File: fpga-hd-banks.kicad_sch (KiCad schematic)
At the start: 16 parts, among them Q4 BSS138PW, Q5 BSS138PW, Q6 BSS138PW, Q7 BSS138PW, Q8 BSS138PW, U34 XCAU25P-2FFVB676I

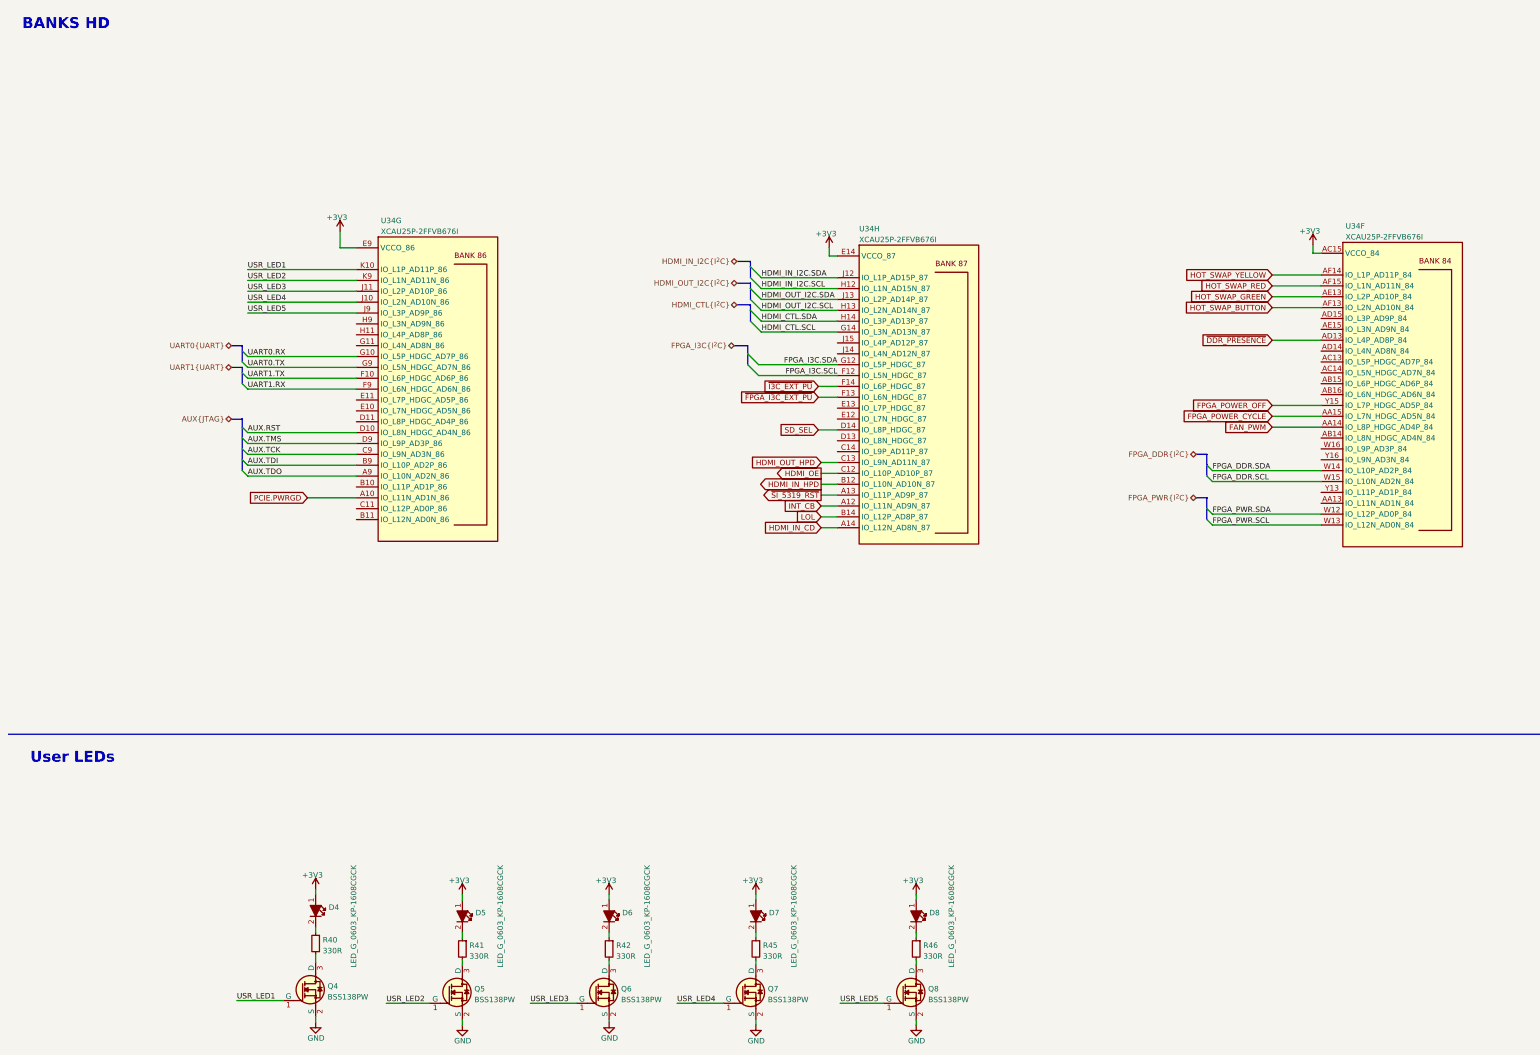
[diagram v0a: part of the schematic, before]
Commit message: [#67725] Clean-up fpga-hd-banks sheet
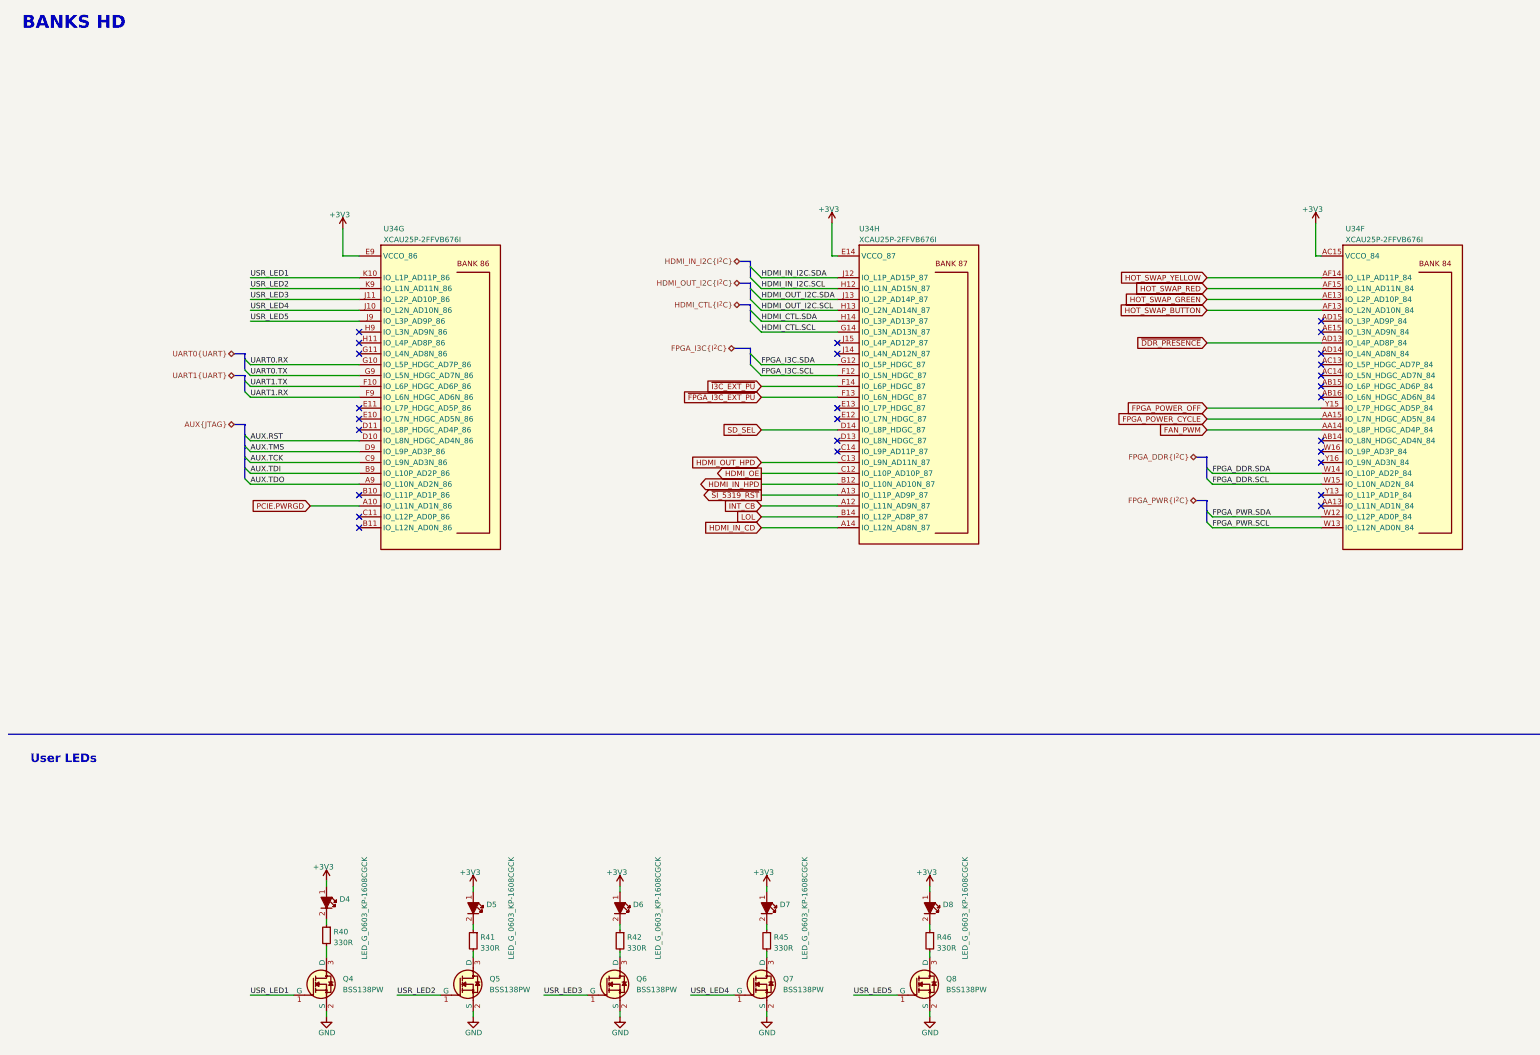
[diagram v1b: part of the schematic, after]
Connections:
- no-connect marks 0 -> 27
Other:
- moved on the sheet: D4, D5, D6, D7, D8, R40, R41, R42, R45, R46, U34F, U34G

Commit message: [#68016] Clean-up the schematic
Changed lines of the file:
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@@
   (title_block
     (title "RDIMM DDR5 Tester")
-    (date "2024-09-26")
+    (date "2024-10")
     (rev "2.0.0")
     (comment 1 "www.antmicro.com")
@@
     (stroke (width 0) (type default))
   )
-  (polyline (pts (xy 12.065 184.15) (xy 407.67 184.15))
-    (stroke (width 0) (type default))
-  )
+  (polyline (pts (xy 12.7 184.15) (xy 407.67 184.15))
+    (stroke (width 0) (type default))
+  )

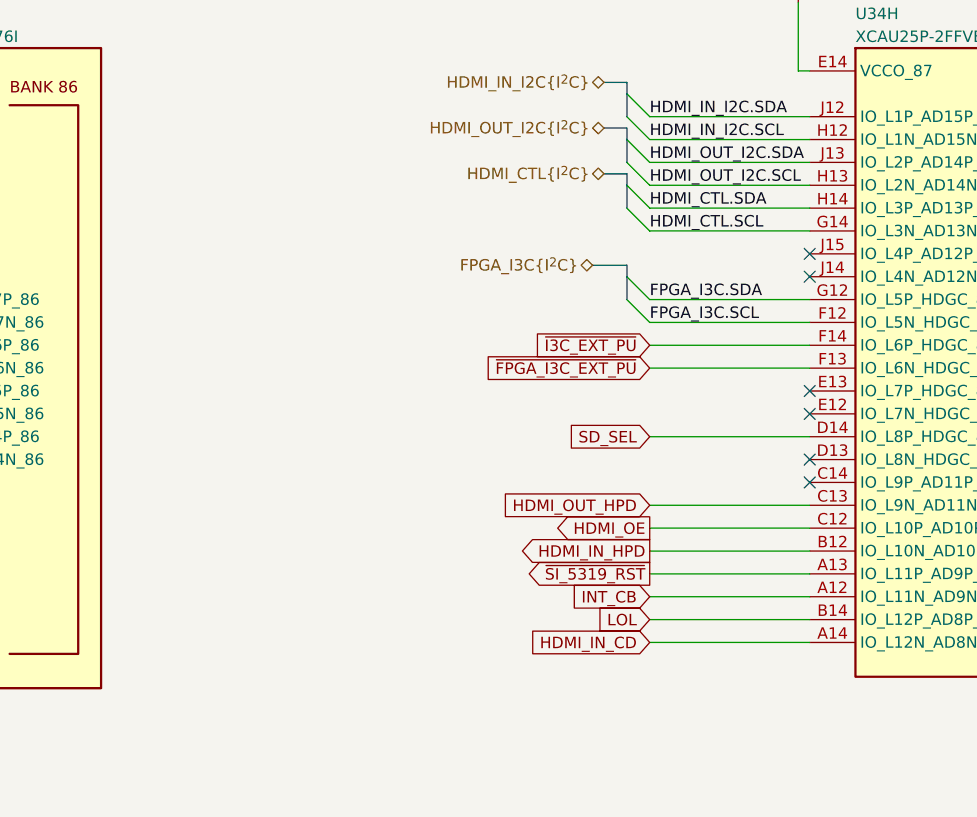
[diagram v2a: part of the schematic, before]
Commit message: [#67408] Update layout for I3C, SDcard and HDMI aux signals
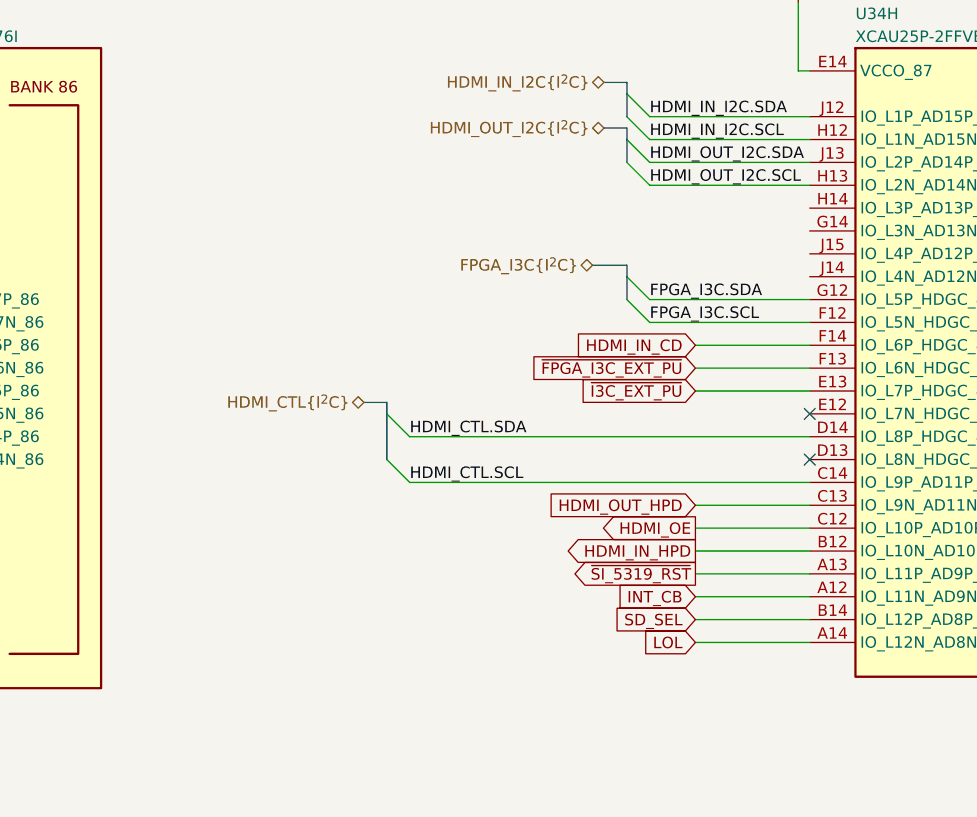
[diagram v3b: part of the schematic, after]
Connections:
- net HDMI_CTL.SCL: now also U34.C14 (IO_L9P_AD11P_87); no longer U34.G14 (IO_L3N_AD13N_87)
- net HDMI_CTL.SDA: now also U34.D14 (IO_L8P_HDGC_87); no longer U34.H14 (IO_L3P_AD13P_87)
- net HDMI_IN_CD: now also U34.F14 (IO_L6P_HDGC_87); no longer U34.A14 (IO_L12N_AD8N_87)
- net LOL: now also U34.A14 (IO_L12N_AD8N_87); no longer U34.B14 (IO_L12P_AD8P_87)
- net SD_SEL: now also U34.B14 (IO_L12P_AD8P_87); no longer U34.D14 (IO_L8P_HDGC_87)
- net ~{I3C_EXT_PU}: now also U34.E13 (IO_L7P_HDGC_87); no longer U34.F14 (IO_L6P_HDGC_87)
- no-connect marks 27 -> 23

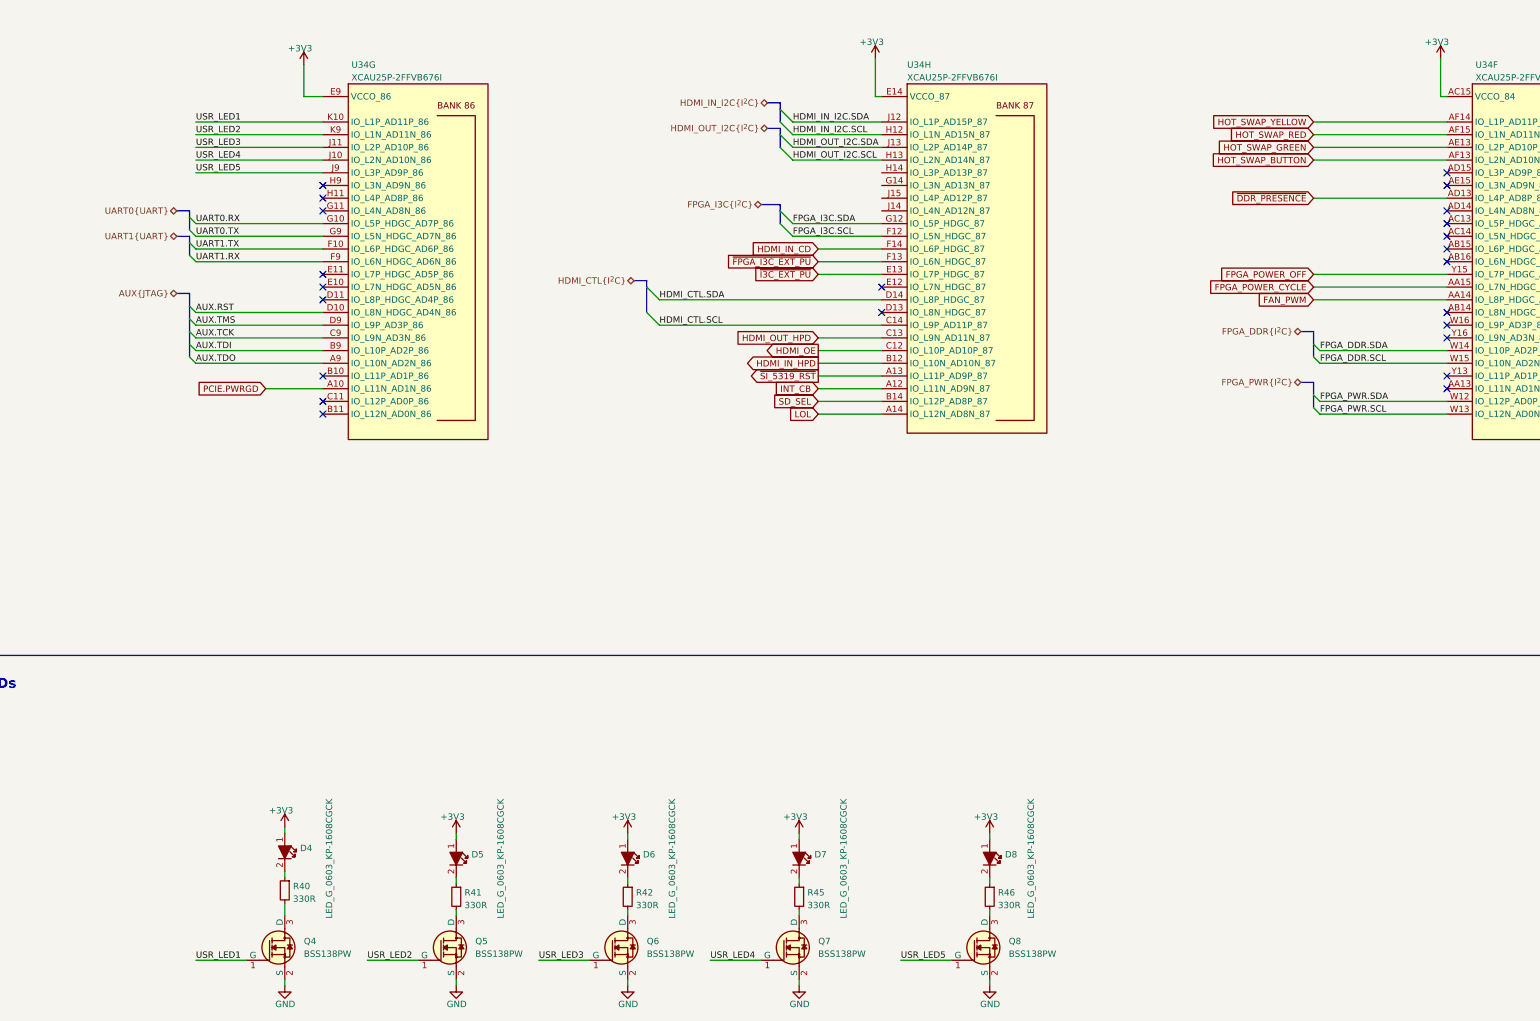
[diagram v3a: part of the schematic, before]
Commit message: [#68016] Improve bus entry marking
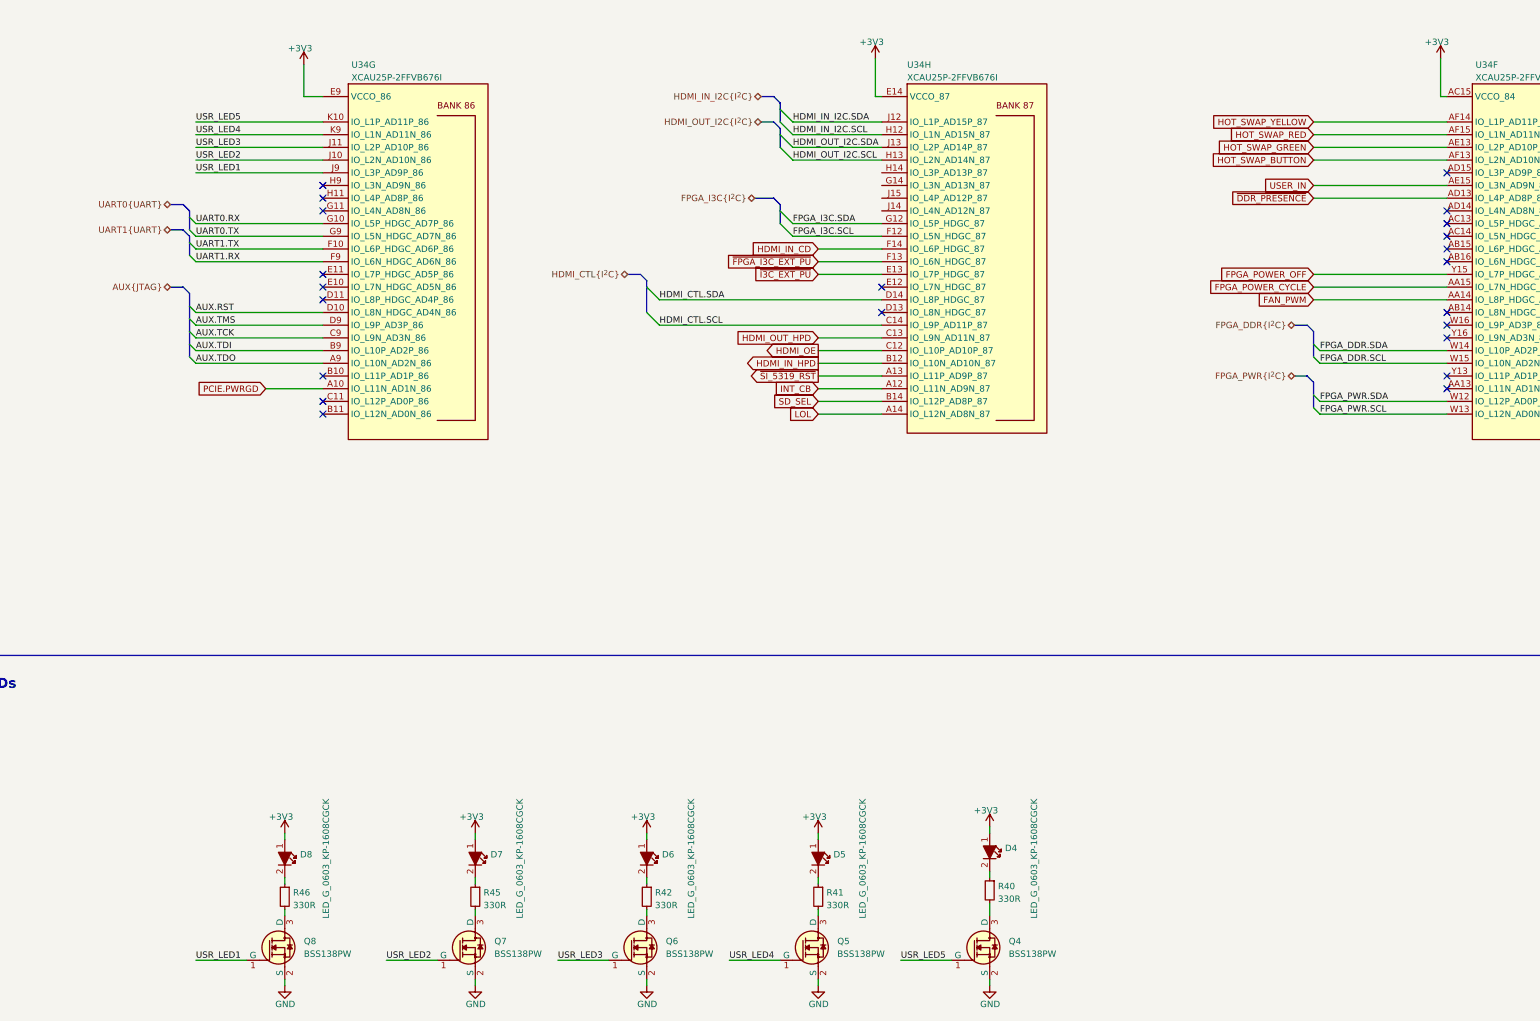
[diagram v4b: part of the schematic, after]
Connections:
- net USR_LED1: now also Q8.1 (G), U34.J9 (IO_L3P_AD9P_86); no longer Q4.1 (G), U34.K10 (IO_L1P_AD11P_86)
- net USR_LED2: now also Q7.1 (G), U34.J10 (IO_L2N_AD10N_86); no longer Q5.1 (G), U34.K9 (IO_L1N_AD11N_86)
- net USR_LED4: now also Q5.1 (G), U34.K9 (IO_L1N_AD11N_86); no longer Q7.1 (G), U34.J10 (IO_L2N_AD10N_86)
- net USR_LED5: now also Q4.1 (G), U34.K10 (IO_L1P_AD11P_86); no longer Q8.1 (G), U34.J9 (IO_L3P_AD9P_86)
- net USER_IN: now reaches U34.AE15 (IO_L3N_AD9N_84)
- no-connect marks 23 -> 22
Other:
- moved on the sheet: D4, D5, D6, D7, D8, Q4, Q5, Q6, Q7, Q8, R40, R41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

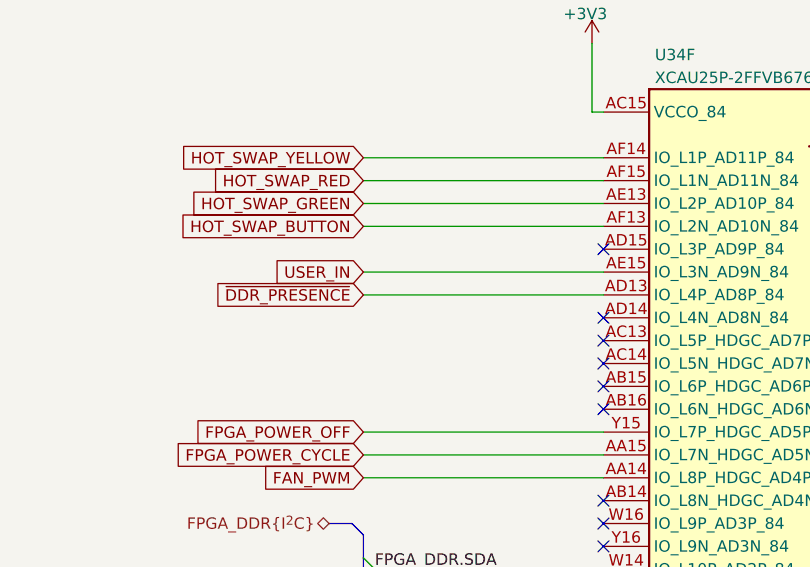
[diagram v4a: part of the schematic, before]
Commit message: [#67824] Finish length matching SPI flash interface. Add DDR5 power control transistors. Finish silkscreen labels replacement
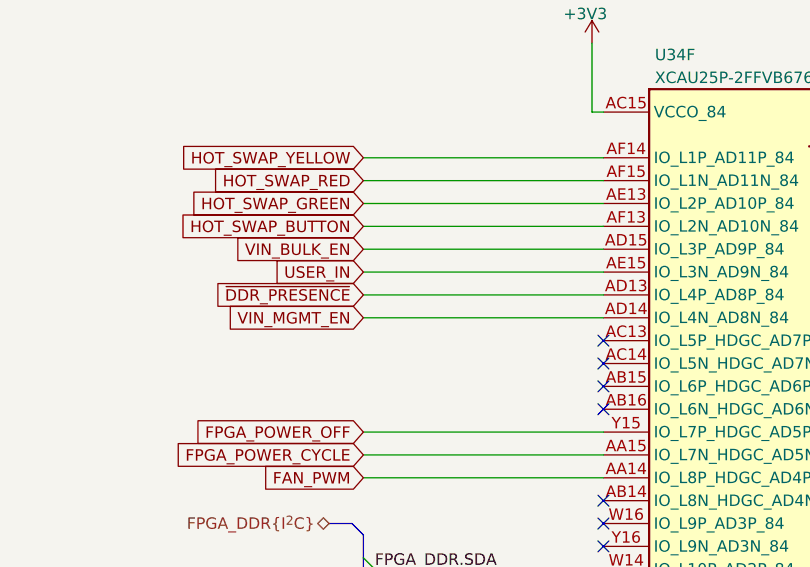
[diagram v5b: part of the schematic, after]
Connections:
- net VIN_MGMT_EN: now reaches U34.AD14 (IO_L4N_AD8N_84)
- net VIN_BULK_EN: now reaches U34.AD15 (IO_L3P_AD9P_84)
- no-connect marks 22 -> 20
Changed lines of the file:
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@@
   )
   (no_connect (at 318.77 120.65))
-  (no_connect (at 318.77 95.25))
   (no_connect (at 93.98 135.89))
   (no_connect (at 93.98 110.49))
@@
   (no_connect (at 93.98 95.25))
   (no_connect (at 93.98 113.03))
-  (no_connect (at 318.77 87.63))
   (no_connect (at 318.77 128.27))
   (no_connect (at 318.77 100.33))
@@
     (stroke (width 0) (type default))
   )
+  (wire (pts (xy 292.1 95.25) (xy 318.77 95.25))
+    (stroke (width 0) (type default))
+  )
   (bus (pts (xy 185.42 78.74) (xy 185.42 80.01))
     (stroke (width 0) (type default))
@@
   )
   (bus (pts (xy 185.42 73.66) (xy 185.42 74.93))
+    (stroke (width 0) (type default))
+  )
+  (wire (pts (xy 292.1 87.63) (xy 318.77 87.63))
     (stroke (width 0) (type default))
   )
@@
     )
   )
+  (global_label "VIN_BULK_EN" (shape input) (at 292.1 87.63 180) (fields_autoplaced)
+    (effects (font (size 1.27 1.27)) (justify right))
+    (property "Intersheetrefs" "${INTERSHEET_REFS}" (at 277.4318 87.63 0)
+      (effects (font (size 1.27 1.27)) (justify right))
+    )
+  )
   (global_label "HOT_SWAP_GREEN" (shape input) (at 292.1 82.55 180) (fields_autoplaced)
     (effects (font (size 1.27 1.27)) (justify right))
@@
       (effects (font (size 1.27 1.27)) (justify right))
     )
+  )
+  (global_label "VIN_MGMT_EN" (shape input) (at 292.1 95.25 180) (fields_autoplaced)
+    (effects (font (size 1.27 1.27)) (justify right))
+    (property "Intersheetrefs" "${INTERSHEET_REFS}" (at 277.19 95.25 0)
+      (effects (font (size 1.27 1.27)) (justify right))
+    )
